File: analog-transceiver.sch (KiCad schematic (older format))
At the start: 139 parts, among them J1 BNC, J2 AF In, J3 AF Out, Q1 2N3904, Q10 2N3904, Q11 2N3904, Q12 2N3904, Q13 2N3904, Q14 2N3904, Q15 2N3904, Q16 2N3904, Q17 2N3904, Q18 BF245A, Q19 2N3906, Q2 2N3904, Q20 2N3904, Q21 BF245A, Q25 BD139, Q26 BD140, Q3 2N3904, SW1 SW_DPDT_x2, SW2 SW_DPDT_x2, T1 Transformer_1P_1S, Y1 10MHz, Y2 10MHz, Y3 10MHz, Y4 10MHz

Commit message: Added L and C values for 10.7Mhz@50ohm diplexer.
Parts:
- C11: value 0 -> 2.7n
- C6: value 0 -> 27p
- L3: value 0 -> 8.2u
- L4: value 0 -> 82n
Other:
- note added: "10.7MHz Diplexer"
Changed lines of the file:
@@
 P 6400 1300
 F 0 "L3" V 6590 1300 50  0000 C CNN
-F 1 "0" V 6499 1300 50  0000 C CNN
+F 1 "8.2u" V 6499 1300 50  0000 C CNN
 F 2 "Inductor_THT:L_Toroid_Vertical_L10.0mm_W5.0mm_P5.08mm" H 6400 1300 50  0001 C CNN
 F 3 "~" H 6400 1300 50  0001 C CNN
@@
 P 6700 1300
 F 0 "C6" V 6448 1300 50  0000 C CNN
-F 1 "0" V 6539 1300 50  0000 C CNN
+F 1 "27p" V 6539 1300 50  0000 C CNN
 F 2 "Potentiometer_THT:Potentiometer_Piher_PT-6-V_Vertical" H 6738 1150 50  0001 C CNN
 F 3 "~" H 6700 1300 50  0001 C CNN
@@
 P 6250 1750
 F 0 "L4" H 6207 1704 50  0000 R CNN
-F 1 "0" H 6207 1795 50  0000 R CNN
+F 1 "82n" H 6207 1795 50  0000 R CNN
 F 2 "Inductor_THT:L_Toroid_Vertical_L10.0mm_W5.0mm_P5.08mm" H 6250 1750 50  0001 C CNN
 F 3 "~" H 6250 1750 50  0001 C CNN
@@
 P 6850 1750
 F 0 "C11" H 6965 1796 50  0000 L CNN
-F 1 "0" H 6965 1705 50  0000 L CNN
+F 1 "2.7n" H 6965 1705 50  0000 L CNN
 F 2 "Capacitor_THT:C_Disc_D3.8mm_W2.6mm_P2.50mm" H 6888 1600 50  0001 C CNN
 F 3 "~" H 6850 1750 50  0001 C CNN
@@
 Wire Wire Line
 	1650 9450 2450 9450
+Text Notes 6300 2300 0    50   ~ 0
+10.7MHz Diplexer
 $EndSCHEMATC

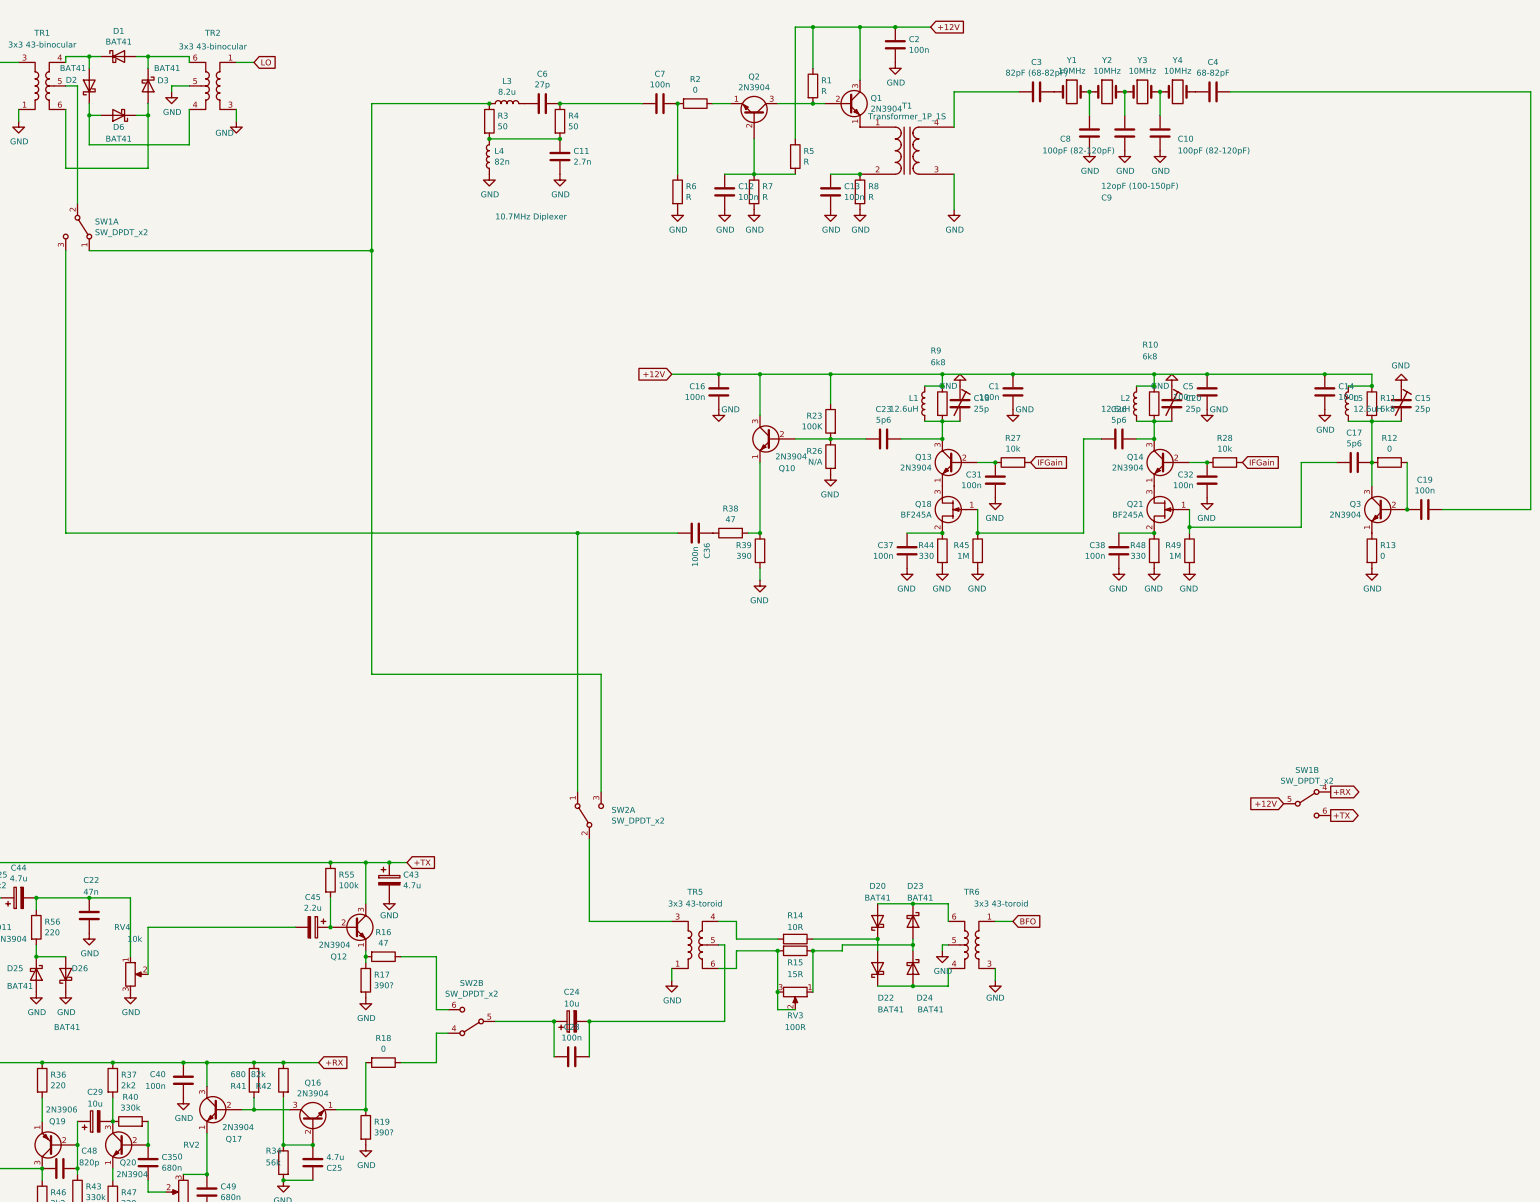
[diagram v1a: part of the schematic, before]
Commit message: Replaced first IF amplifier after diplexer. Changed matching network for IN and OUT of the IF filter. Removed first amplifier stage after the IF filter. Added audio diplexer after the BFO mixer.
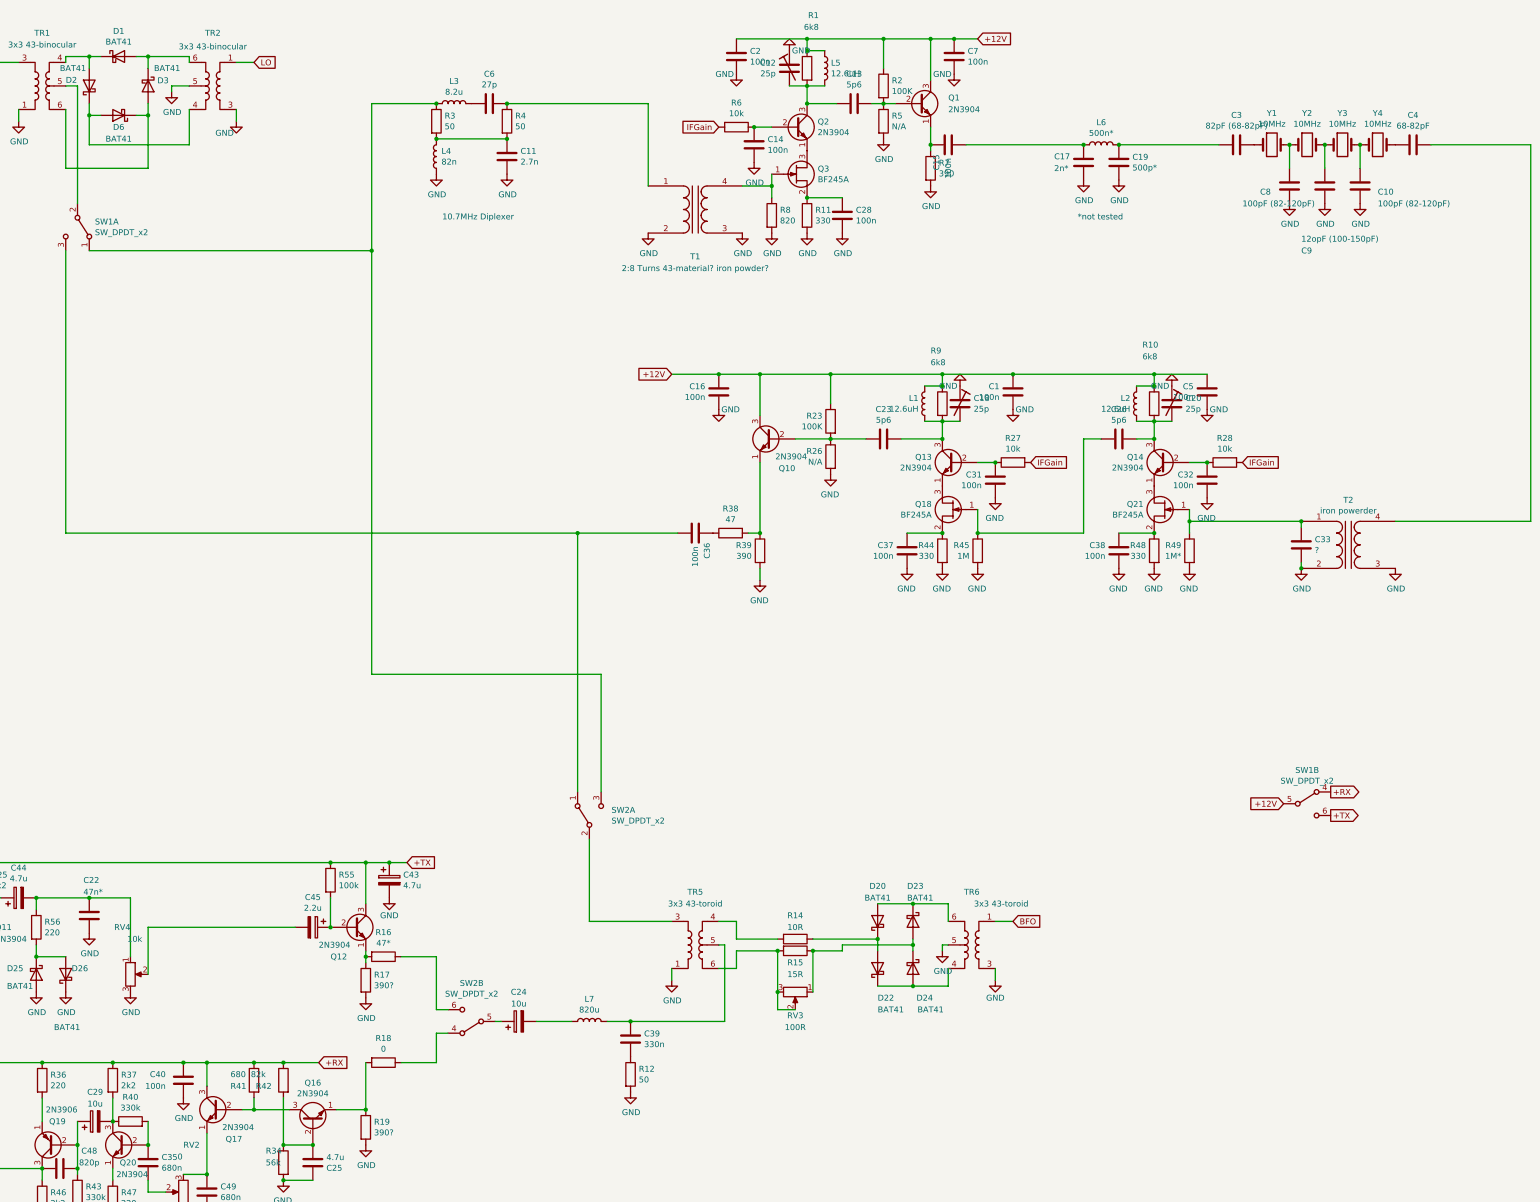
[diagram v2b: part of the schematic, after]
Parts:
- removed C12: 100n, Capacitor_THT:C_Disc_D3.8mm_W2.6mm_P2.50mm, symbol Device:C
- removed C15: 25p, Potentiometer_THT:Potentiometer_Piher_PT-6-V_Vertical, symbol Device:CTRIM
- removed Q3: 2N3904, Package_TO_SOT_THT:TO-92_Inline_Wide, symbol Transistor_BJT:2N3904
- removed R13: 0, Resistor_THT:R_Axial_DIN0204_L3.6mm_D1.6mm_P5.08mm_Horizontal, symbol Device:R
- added C12: 25p, Potentiometer_THT:Potentiometer_Piher_PT-6-V_Vertical, symbol Device:CTRIM
- added C15: 100n, Capacitor_THT:C_Disc_D3.8mm_W2.6mm_P2.50mm, symbol Device:C
- added C33: ?, symbol Device:C
- added C39: 330n, symbol Device:C
- added L6: 500n*, symbol Device:L
- added L7: 820u, symbol Device:L
- added Q3: BF245A, Package_TO_SOT_THT:TO-92_Inline_Wide, symbol Transistor_FET:BF245A
- added T2: iron powerder, symbol Device:Transformer_1P_1S
- C13: value 100n -> 5p6
- C17: value 5p6 -> 2n*; footprint Capacitor_THT:C_Disc_D3.8mm_W2.6mm_P2.50mm -> (none)
- C19: value 100n -> 500p*; footprint Capacitor_THT:C_Disc_D3.8mm_W2.6mm_P2.50mm -> (none)
- C22: value 47n -> 47n*
- R1: value R -> 6k8
- R11: value 6k8 -> 330
- R12: value 0 -> 50; footprint Resistor_THT:R_Axial_DIN0207_L6.3mm_D2.5mm_P2.54mm_Vertical -> (none)
- R16: value 47 -> 47*
- R2: value 0 -> 100K
- R49: value 1M -> 1M*
- R5: value R -> N/A; footprint Resistor_THT:R_Axial_DIN0207_L6.3mm_D2.5mm_P2.54mm_Vertical -> Resistor_THT:R_Axial_DIN0204_L3.6mm_D1.6mm_P5.08mm_Horizontal
- R6: value R -> 10k; footprint Resistor_THT:R_Axial_DIN0204_L3.6mm_D1.6mm_P5.08mm_Horizontal -> Resistor_THT:R_Axial_DIN0207_L6.3mm_D2.5mm_P2.54mm_Vertical
- R7: value R -> 390; footprint Resistor_THT:R_Axial_DIN0207_L6.3mm_D2.5mm_P2.54mm_Vertical -> Resistor_THT:R_Axial_DIN0204_L3.6mm_D1.6mm_P5.08mm_Horizontal
- R8: value R -> 820; footprint Resistor_THT:R_Axial_DIN0207_L6.3mm_D2.5mm_P2.54mm_Vertical -> Resistor_THT:R_Axial_DIN0204_L3.6mm_D1.6mm_P5.08mm_Horizontal
- T1: value Transformer_1P_1S -> 2:8 Turns 43-material? iron powder?; footprint Button_Switch_THT:SW_NKK_G1xJP -> (none)
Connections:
- net +12V: now also C7.1, L5.1, R2.1; no longer C14.1, L5.2, R11.1, R5.1
- net GND: now also C17.2, C19.2, C28.2, C7.2, R11.2, R12.2, R5.2, T1.2 (AB), C12.1, C33.2, T2.2 (AB), T2.3 (SA); no longer C13.2, R6.2
- net IFGain: now also R6.2
- net at C3.2: now also C19.1, L6.2; no longer T1.4 (SB)
- net at C4.1: now also T2.4 (SB); no longer C19.1
- net at C24.1, SW2.5 (B): no longer C28.2
- net at Q21.1 (G), R49.1: now also C33.1, T2.1 (AA); no longer C17.2
- net at R12.1: now also C39.2; no longer C19.2
- net at T1.1 (AA): now also C6.1, R4.1; no longer Q1.1 (E)
- net at Q2.3 (C), R1.2: now also C13.2, L5.2, C12.2; no longer Q1.2 (B)
- net at Q2.1 (E): now also Q3.3 (D); no longer R2.1
- new net: C39.1, L7.2, TR5.5
- new net: C24.2, L7.1
- new net: C15.1, Q1.1 (E), R7.1
- new net: C13.1, Q1.2 (B), R2.2, R5.1
- new net: C15.2, C17.1, L6.1
- new net: Q3.1 (G), R8.1, T1.4 (SB)
- new net: C28.1, Q3.2 (S), R11.1
- new net: C14.1, Q2.2 (B), R6.1
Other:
- note added: "*not tested"
- moved on the sheet: C10, C11, C24, C3, C4, C6, C8, C9, L3, L4, R3, R4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

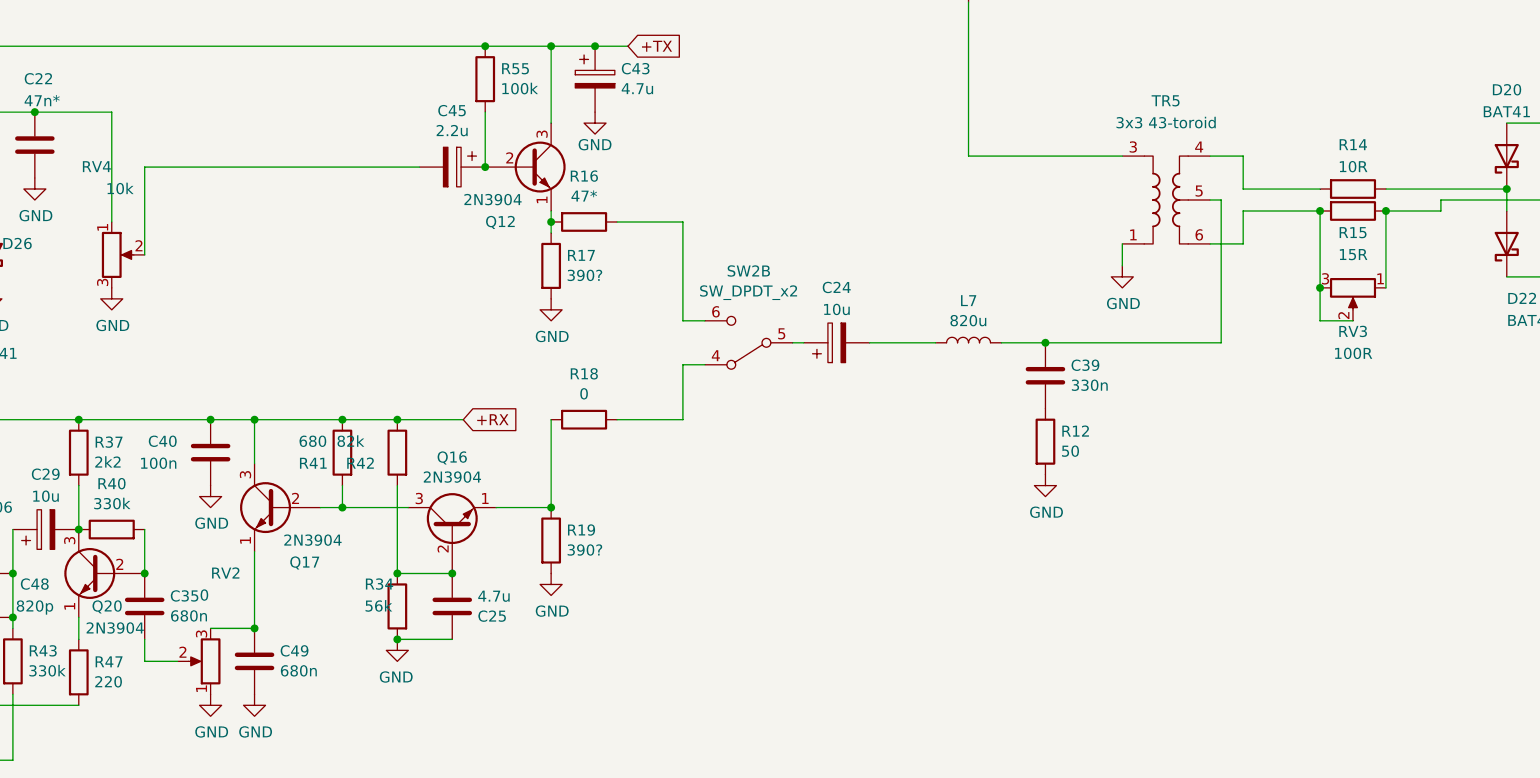
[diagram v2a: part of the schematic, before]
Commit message: Changed component values for Rx audio pre-amp. to match 50ohms without adapter circuit. Changed balance resistor values at BFO mixer.
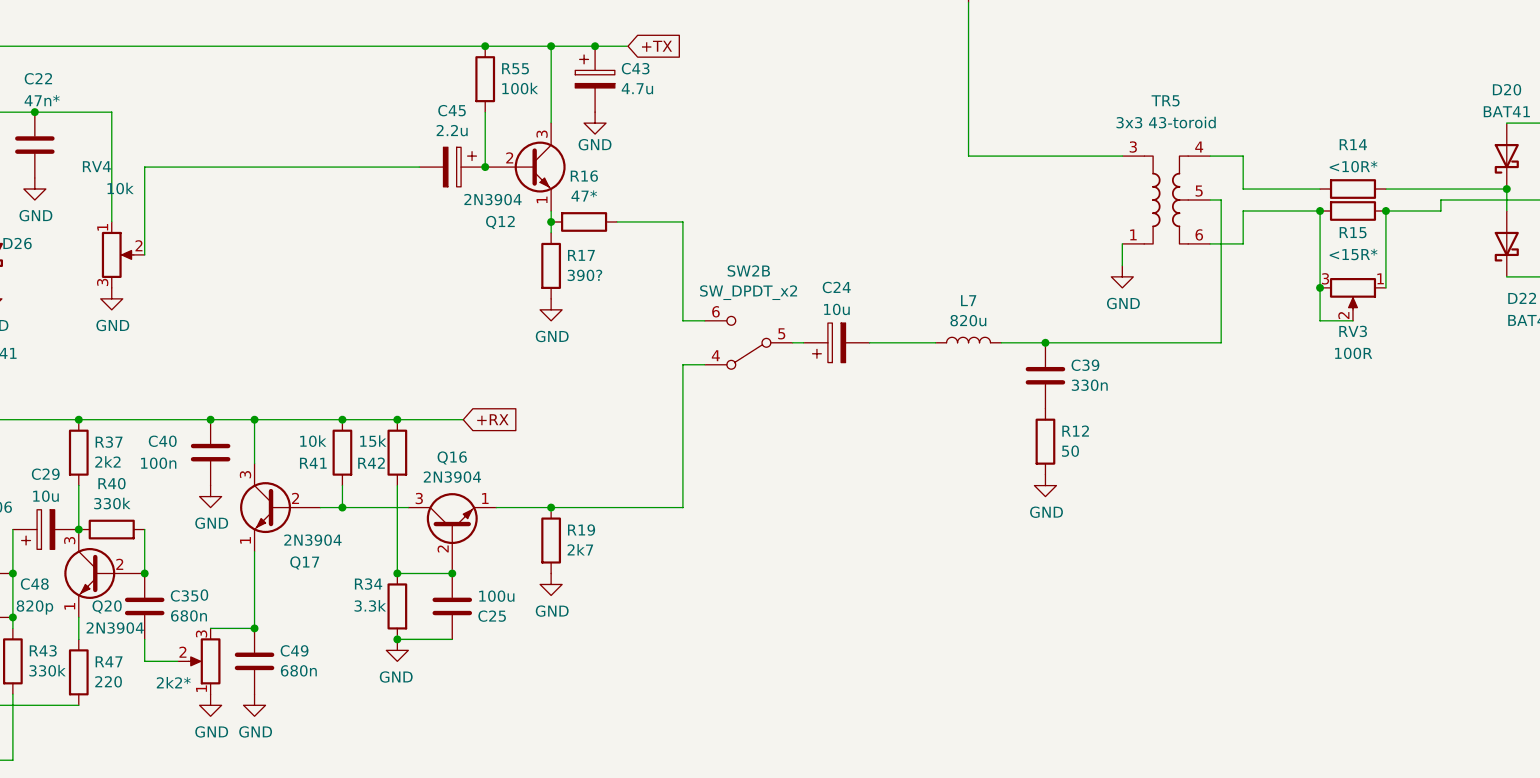
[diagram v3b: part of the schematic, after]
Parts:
- removed R18: 0, Resistor_THT:R_Axial_DIN0204_L3.6mm_D1.6mm_P5.08mm_Horizontal, symbol Device:R
- C25: value 4.7u -> 100u
- R14: value 10R -> <10R*
- R15: value 15R -> <15R*
- R19: value 390? -> 2k7
- R34: value 56k -> 3.3k
- R41: value 680 -> 10k
- R42: value 82k -> 15k
- renumbered RV2 to 2k2*
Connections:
- net at Q16.1 (E), R19.1: now also SW2.4 (A)
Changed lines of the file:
@@
 P 4250 9600
 F 0 "R41" H 4450 9550 50  0000 R CNN
-F 1 "680" H 4450 9650 50  0000 R CNN
+F 1 "10k" H 4450 9650 50  0000 R CNN
 F 2 "Resistor_THT:R_Axial_DIN0204_L3.6mm_D1.6mm_P5.08mm_Horizontal" V 4180 9600 50  0001 C CNN
 F 3 "~" H 4250 9600 50  0001 C CNN
@@
 P 4750 10300
 F 0 "C25" H 4635 10254 50  0000 R CNN
-F 1 "4.7u" H 4635 10345 50  0000 R CNN
+F 1 "100u" H 4635 10345 50  0000 R CNN
 F 2 "Capacitor_THT:C_Disc_D3.8mm_W2.6mm_P2.50mm" H 4788 10150 50  0001 C CNN
 F 3 "~" H 4750 10300 50  0001 C CNN
@@
 U 1 1 5F521291
 P 4500 9600
-F 0 "R42" H 4600 9550 50  0000 L CNN
-F 1 "82k" H 4650 9650 50  0000 L CNN
+F 0 "R42" H 4550 9550 50  0000 L CNN
+F 1 "15k" H 4550 9650 50  0000 L CNN
 F 2 "Resistor_THT:R_Axial_DIN0207_L6.3mm_D2.5mm_P2.54mm_Vertical" V 4430 9600 50  0001 C CNN
 F 3 "~" H 4500 9600 50  0001 C CNN
@@
 $EndComp
 $Comp
-L Device:R_POT RV2
+L Device:R_POT 2k2*
 U 1 1 5FB97227
 P 3650 10550
-F 0 "RV2" H 3650 10150 50  0000 R CNN
+F 0 "2k2*" H 3900 10650 50  0000 R CNN
 F 1 "0" H 3700 10250 50  0000 R CNN
 F 2 "Potentiometer_THT:Potentiometer_Vishay_T73XW_Horizontal" H 3650 10550 50  0001 C CNN
@@
 U 1 1 5F5211E6
 P 4500 10300
-F 0 "R34" H 4650 10400 50  0000 R CNN
-F 1 "56k" H 4650 10300 50  0000 R CNN
+F 0 "R34" H 4700 10400 50  0000 R CNN
+F 1 "3.3k" H 4700 10300 50  0000 R CNN
 F 2 "Resistor_THT:R_Axial_DIN0207_L6.3mm_D2.5mm_P2.54mm_Vertical" V 4430 10300 50  0001 C CNN
 F 3 "~" H 4500 10300 50  0001 C CNN
@@
 Wire Wire Line
 	4950 9850 5200 9850
-Wire Wire Line
-	5200 9450 5200 9850
 $Comp
 L Device:C C48
@@
 P 5200 10000
 F 0 "R19" H 5270 10046 50  0000 L CNN
-F 1 "390?" H 5270 9955 50  0000 L CNN
+F 1 "2k7" H 5270 9955 50  0000 L CNN
 F 2 "Resistor_THT:R_Axial_DIN0204_L3.6mm_D1.6mm_P5.08mm_Horizontal" V 5130 10000 50  0001 C CNN
 F 3 "~" H 5200 10000 50  0001 C CNN
 	1    5200 10000
 	1    0    0    -1
-$EndComp
-Connection ~ 5200 9850
-$Comp
-L Device:R R18
-U 1 1 6290EA84
-P 5350 9450
-F 0 "R18" V 5143 9450 50  0000 C CNN
-F 1 "0" V 5234 9450 50  0000 C CNN
-F 2 "Resistor_THT:R_Axial_DIN0204_L3.6mm_D1.6mm_P5.08mm_Horizontal" V 5280 9450 50  0001 C CNN
-F 3 "~" H 5350 9450 50  0001 C CNN
-	1    5350 9450
-	0    1    1    0
 $EndComp
 $Comp
@@
 	5800 8550 5500 8550
 Wire Wire Line
-	5500 9450 5800 9450
-Wire Wire Line
-	5800 9450 5800 9200
-Wire Wire Line
 	5800 9200 5900 9200
 Wire Wire Line
@@
 P 8850 8400
 F 0 "R14" V 8650 8400 50  0000 C CNN
-F 1 "10R" V 8750 8400 50  0000 C CNN
+F 1 "<10R*" V 8750 8400 50  0000 C CNN
 F 2 "Resistor_THT:R_Axial_DIN0204_L3.6mm_D1.6mm_P5.08mm_Horizontal" V 8780 8400 50  0001 C CNN
 F 3 "~" H 8850 8400 50  0001 C CNN
@@
 P 8850 8500
 F 0 "R15" V 8950 8500 50  0000 C CNN
-F 1 "15R" V 9050 8500 50  0000 C CNN
+F 1 "<15R*" V 9050 8500 50  0000 C CNN
 F 2 "Resistor_THT:R_Axial_DIN0204_L3.6mm_D1.6mm_P5.08mm_Horizontal" V 8780 8500 50  0001 C CNN
 F 3 "~" H 8850 8500 50  0001 C CNN
@@
 Wire Wire Line
 	7250 9100 7450 9100
+Wire Wire Line
+	5200 9850 5800 9850
+Wire Wire Line
+	5800 9200 5800 9850
+Connection ~ 5200 9850
 $EndSCHEMATC
